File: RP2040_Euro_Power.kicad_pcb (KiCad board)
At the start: 2 copper layers, 110 x 110 mm, 150 parts, among them J1 Conn_01x40, J2 Conn_01x40, J3 Power, J4 USB C/USB 2.0, J5 Conn_01x03_Pin, SW1 SW_BOOT, SW2 SW_RESET, U1 78L05_SOT89, U101 TL431A, U2 W25Q128JVS, U4 AMS1117-3.3, U5 RP2040, U7 TL072, Y1 Crystal_12MHz_4Pin

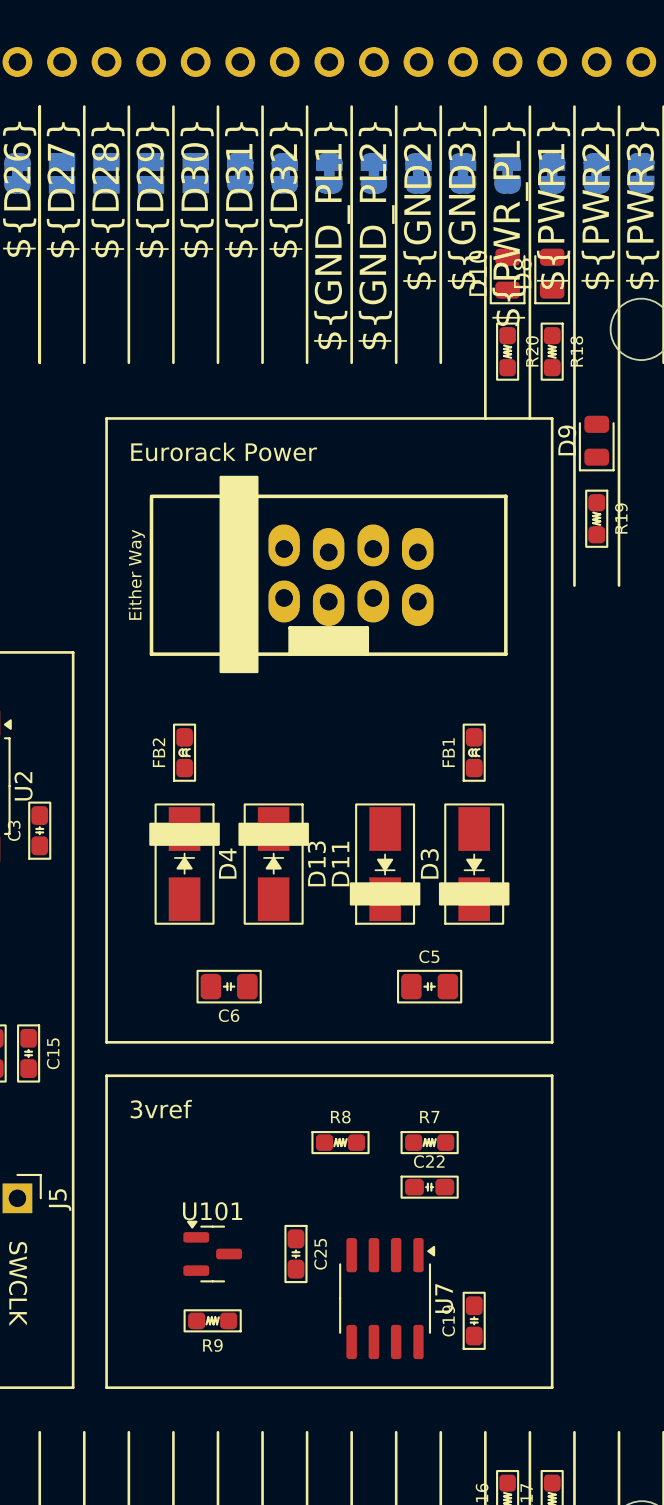
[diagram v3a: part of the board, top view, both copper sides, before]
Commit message: Second op amp used. Ready for routing
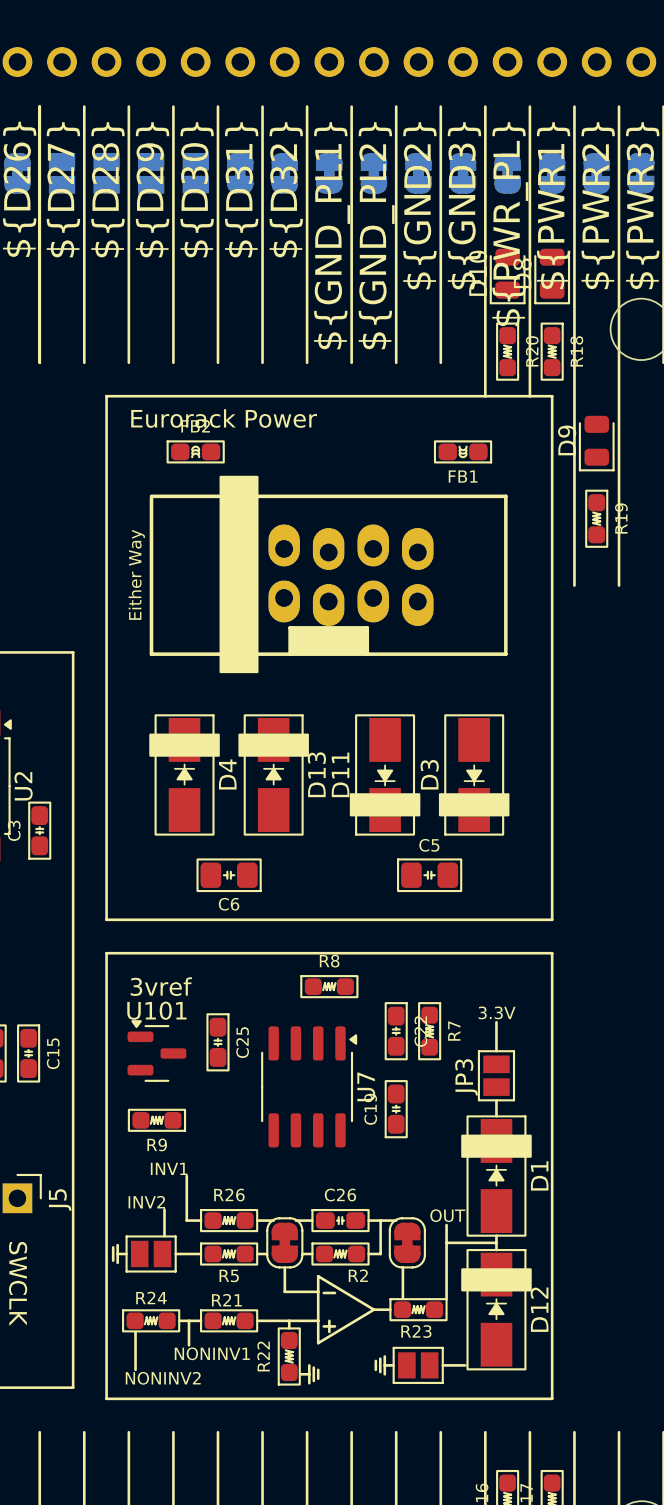
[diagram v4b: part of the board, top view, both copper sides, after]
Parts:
- added C26: DNP, winterbloom:C_0603_HandSolder, F.Cu at (161.3, 109.7)
- added D1: D_Schottky, winterbloom:D_SMA, F.Cu at (170.2, 107.1)
- added D12: D_Schottky, winterbloom:D_SMA, F.Cu at (170.2, 114.8)
- added JP1: Jumper_Closed, Jumper:SolderJumper-2_P1.3mm_Bridged_RoundedPad1.0x1.5mm, F.Cu at (158.2, 111.0)
- added JP2: SolderJumper_2_Open, Jumper:SolderJumper-2_P1.3mm_Open_Pad1.0x1.5mm, F.Cu at (150.5, 111.6)
- added JP201: Jumper_Closed, Jumper:SolderJumper-2_P1.3mm_Bridged_RoundedPad1.0x1.5mm, F.Cu at (165.2, 111.0)
- added JP3: SolderJumper_2_Open, Jumper:SolderJumper-2_P1.3mm_Open_Pad1.0x1.5mm, F.Cu at (170.2, 101.4)
- added JP4: SolderJumper_2_Open, Jumper:SolderJumper-2_P1.3mm_Open_Pad1.0x1.5mm, F.Cu at (165.8, 117.9)
- added R2: DNP, winterbloom:R_0603_HandSolder, F.Cu at (161.3, 111.6)
- added R21: DNP, winterbloom:R_0603_HandSolder, F.Cu at (155.0, 115.4)
- added R22: DNP, winterbloom:R_0603_HandSolder, F.Cu at (158.4, 117.4)
- added R23: DNP, winterbloom:R_0603_HandSolder, F.Cu at (165.8, 114.8)
- added R24: DNP, winterbloom:R_0603_HandSolder, F.Cu at (150.5, 115.4)
- added R26: DNP, winterbloom:R_0603_HandSolder, F.Cu at (155.0, 109.7)
- added R5: DNP, winterbloom:R_0603_HandSolder, F.Cu at (155.0, 111.6)
- moved FB1 17.2 mm to (168.3, 65.9), turned to 180 degrees
- moved FB2 17.2 mm to (153.1, 65.9), turned to 0 degrees
- moved C19 12.9 mm to (164.5, 103.3)
- moved C25 12.9 mm to (154.4, 99.5)
- moved U7 12.9 mm to (159.4, 102.1)
- moved R9 11.9 mm to (150.9, 104.0)
- moved U101 11.9 mm to (150.9, 100.2)
- moved C22 9.09 mm to (164.5, 98.9), turned to -90 degrees
- moved R8 8.91 mm to (160.7, 96.3)
- moved C5 6.35 mm to (166.4, 90.0)
- moved C6 6.35 mm to (155.0, 90.0)
- moved R7 6.35 mm to (166.4, 98.9), turned to -90 degrees
- moved D11 5.08 mm to (163.9, 84.3)
- moved D13 5.08 mm to (157.5, 84.3)
- moved D3 5.08 mm to (169.0, 84.3)
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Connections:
- U2 pad 1: Net-(U2-~{CS}) -> QSPI_CS
- U5 pad 56: Net-(U2-~{CS}) -> QSPI_CS
- U7 pad 5: GND_PLANE -> Net-(U7B-+)
- U7 pad 6: Net-(U7B--) -> Net-(JP1-A)
- U7 pad 7: Net-(U7B--) -> Net-(JP201-A)
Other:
- board text added: "3.3V"
- board text added: "INV1"
- board text added: "INV2"
- board text added: "NONINV1"
- board text added: "NONINV2"
- board text added: "OUT"

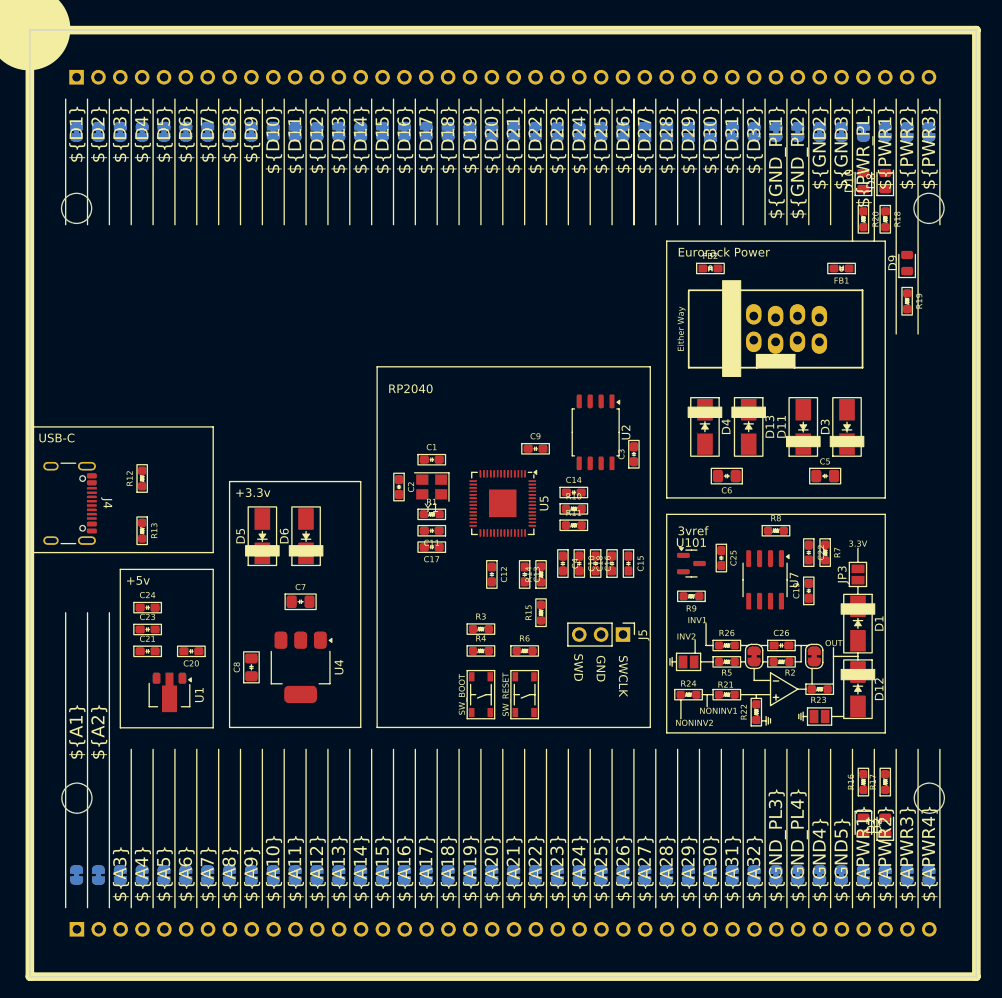
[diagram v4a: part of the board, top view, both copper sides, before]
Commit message: First draft of routing done. Still need to clean everything up, but it passes DRC.
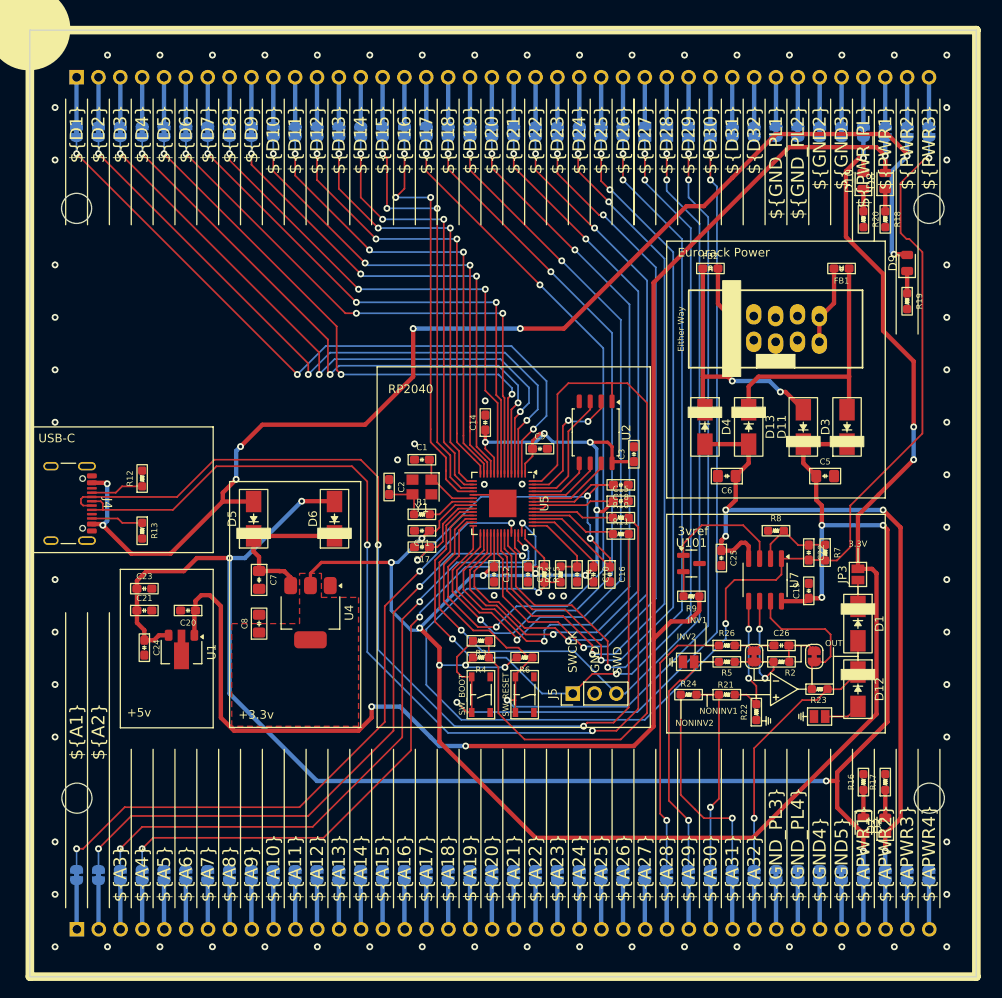
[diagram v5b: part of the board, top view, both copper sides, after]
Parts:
- moved C14 13.1 mm to (126.9, 83.8), turned to 90 degrees
- moved C18 9.20 mm to (142.7, 91.0), turned to 180 degrees
- moved J5 9.01 mm to (137.1, 115.3), turned to 90 degrees
- moved C15 7.29 mm to (142.7, 92.9), turned to 0 degrees
- moved U4 6.45 mm to (106.6, 105.9)
- moved R10 5.55 mm to (142.7, 94.8)
- moved R11 5.55 mm to (142.7, 96.7)
- moved C7 5.45 mm to (100.6, 102.1), turned to -90 degrees
- moved U1 5.19 mm to (91.6, 110.4)
- moved C8 5.16 mm to (100.6, 107.1)
- moved C20 4.76 mm to (92.4, 105.6)
- moved C21 4.76 mm to (87.3, 105.6)
- moved C23 4.76 mm to (87.3, 103.1)
- moved C24 4.67 mm to (87.3, 109.9), turned to -90 degrees
- moved R15 4.46 mm to (133.8, 101.4), turned to -90 degrees
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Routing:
- net IOVDD: track 0.00 -> 308.1 mm, vias 0 -> 16
- net APWR1: track 0.00 -> 207.4 mm, vias 0 -> 7
- net PWR1: track 0.00 -> 174.3 mm, vias 0 -> 3
- net PWR2: track 0.00 -> 149.8 mm, vias 0 -> 8
- net 3VREF: track 0.00 -> 142.9 mm, vias 0 -> 3
- net D29: track 0.00 -> 118.0 mm, vias 0 -> 3
- net USBD+: track 0.00 -> 116.0 mm, vias 0 -> 2
- net USBD-: track 0.00 -> 113.1 mm, vias 0 -> 2
- net D27: track 0.00 -> 110.2 mm, vias 0 -> 4
- net D28: track 0.00 -> 108.7 mm, vias 0 -> 3
- net BOOT: track 0.00 -> 105.1 mm, vias 0 -> 3
- net D26: track 0.00 -> 92.1 mm, vias 0 -> 3
- net D20: track 0.00 -> 91.6 mm, vias 0 -> 3
- net D17: track 0.00 -> 91.4 mm, vias 0 -> 3
- net QSPI_CS: track 0.00 -> 91.3 mm
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- added copper zone on F.Cu, net IOVDD

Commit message: Loom RP2040 V1 Ordered
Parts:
- JP101, JP102, JP103, JP104, JP105, JP106, JP107, JP108, JP109, JP110, JP111, JP112, JP113, JP114, JP115, JP116, JP117, JP118, JP119, JP120, JP121, JP122, JP123, JP124, JP125, JP126, JP131, JP132, JP133, JP134, JP135, JP136, JP137, JP138, JP139, JP140, JP141, JP142, JP143, JP144, JP145, JP146, JP147, JP148, JP149, JP150, JP151, JP152, JP153, JP154, JP155, JP156, JP157, JP158, JP159, JP160, JP161, JP162, JP163, JP164, JP165, JP166, JP167, JP168, JP169, JP170, JP171, JP172, JP173, JP174, JP175, JP176, JP177, JP178, JP179, JP180: footprint Jumper:SolderJumper-2_P1.3mm_Bridged_RoundedPad1.0x1.5mm -> Decapod_Devices:SolderJumper-2_P1.3mm_Bridged_RoundedPad1.0x1.5mm
- JP127, JP128, JP129, JP130: footprint Jumper:SolderJumper-2_P1.3mm_Open_Pad1.0x1.5mm -> Decapod_Devices:SolderJumper-2_P1.3mm_Open_Pad1.0x1.5mm
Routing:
- net PWR2: track 149.8 -> 145.3 mm
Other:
- board text added: "Add more GND Vias clean up ref des add any silk markings? add test points?"
- board text added: "TODO"

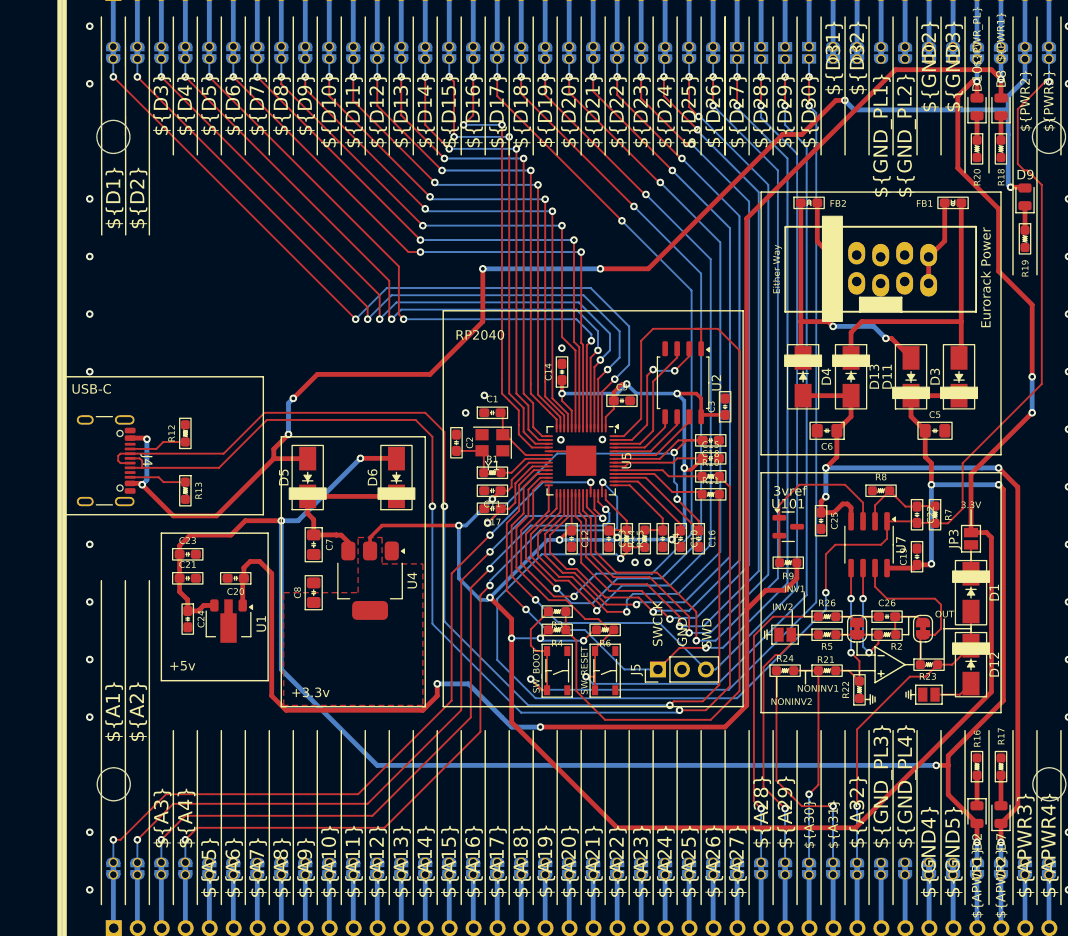
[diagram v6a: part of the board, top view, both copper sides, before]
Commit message: Moved buttons to the side, disconnected opamp
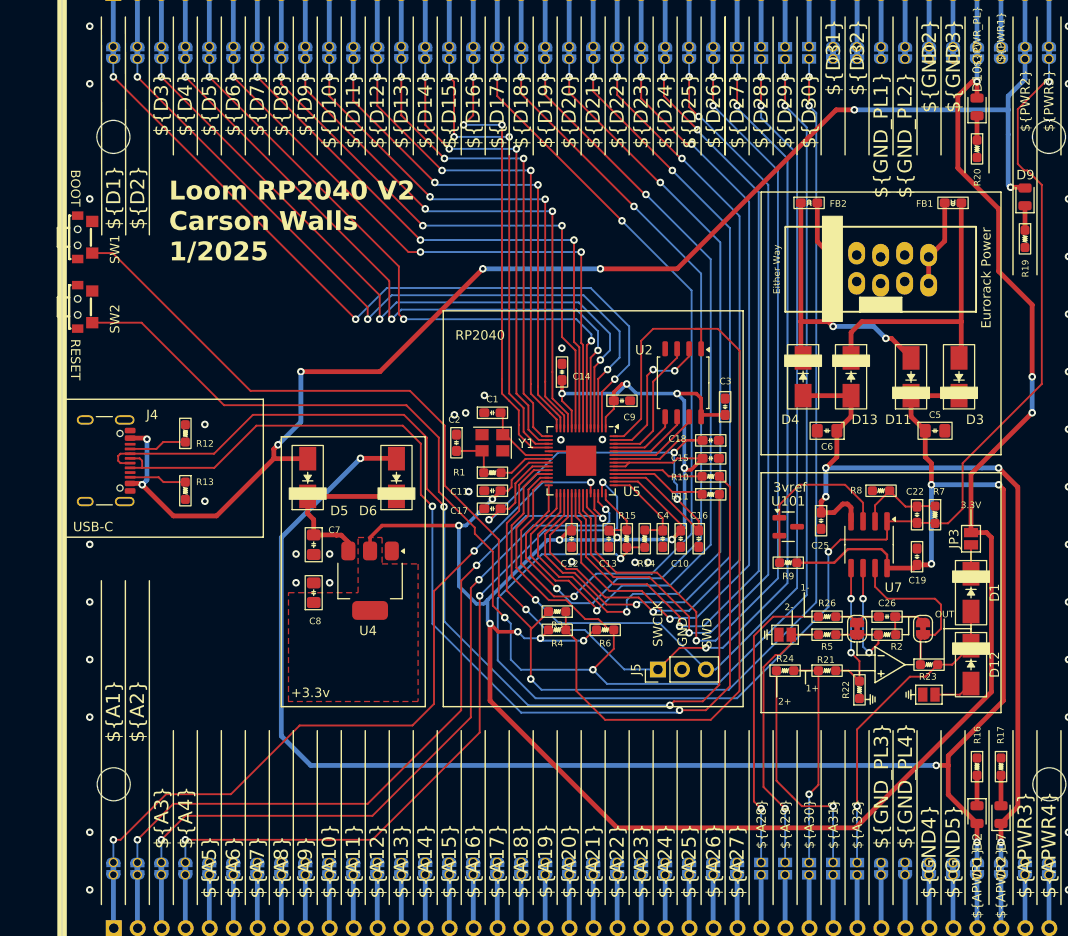
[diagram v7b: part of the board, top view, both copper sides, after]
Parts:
- removed C20, C21, C23, C24: 100n, winterbloom:C_0603_HandSolder
- removed D8: 5v, LED_SMD:LED_0805_2012Metric
- removed R18: 1k, winterbloom:R_0603_HandSolder
- removed U1: 78L05_SOT89, Package_TO_SOT_SMD:SOT-89-3
- JP168, JP169, JP170, JP171, JP172: value ~ -> SolderJumper_2_Open; footprint Decapod_Devices:SolderJumper-2_P1.3mm_Bridged_RoundedPad1.0x1.5mm -> Decapod_Devices:SolderJumper-2_P1.3mm_Open_Pad1.0x1.5mm
- R16, R17: value 3.3k -> 10k
- R19: value 1k -> 3.3k
- R20: value 470R -> 1k
- SW1: value SW_BOOT -> BOOT; footprint winterbloom:Tactile_Switch_4.2mm -> Decapod_Devices:SW-SMD_TS24CA
- SW2: value SW_RESET -> RESET; footprint winterbloom:Tactile_Switch_4.2mm -> Decapod_Devices:SW-SMD_TS24CA
- moved SW1 67.9 mm to (76.4, 69.5)
- moved SW2 67.2 mm to (76.4, 76.9)
- turned JP168 to 90 degrees
- turned JP169 to 90 degrees
- turned JP170 to 90 degrees
- turned JP171 to 90 degrees
- turned JP172 to 90 degrees
- turned R16 to -90 degrees
- turned R17 to -90 degrees
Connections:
- JP168 pad 1: A28 -> Net-(J2-Pin_28)
- JP168 pad 2: Net-(J2-Pin_28) -> A28
- JP169 pad 1: A29 -> Net-(J2-Pin_29)
- JP169 pad 2: Net-(J2-Pin_29) -> A29
- JP170 pad 1: A30 -> Net-(J2-Pin_30)
- JP170 pad 2: Net-(J2-Pin_30) -> A30
- JP171 pad 1: A31 -> Net-(J2-Pin_31)
- JP171 pad 2: Net-(J2-Pin_31) -> A31
- JP172 pad 1: A32 -> Net-(J2-Pin_32)
- JP172 pad 2: Net-(J2-Pin_32) -> A32
- R16 pad 1: Net-(D2-K) -> GND_PLANE
- R16 pad 2: GND_PLANE -> Net-(D2-K)
- R17 pad 1: Net-(D7-A) -> GND_PLANE
- R17 pad 2: GND_PLANE -> Net-(D7-A)
- R9 pad 1: PWR1 -> APWR1
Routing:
- net PWR1: track 174.3 -> 0.00 mm, vias 3 -> 0
- net D29: track 118.0 -> 192.0 mm, vias 3 -> 4
- net BOOT: track 105.1 -> 170.5 mm
- net APWR1: track 207.4 -> 200.0 mm, vias 7 -> 6
- net IOVDD: track 308.1 -> 311.7 mm
- net PWR2: track 145.3 -> 142.3 mm
- net Net-(D8-K): track 2.59 -> 0.00 mm
- net USBD+: track 116.0 -> 114.4 mm
- net USBD-: track 113.1 -> 111.5 mm
- net A1: track 77.7 -> 76.8 mm
- net DVDD: track 67.5 -> 66.8 mm
- net GND_PLANE: vias 70 -> 75
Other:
- board text added: "1+"
- board text added: "1-"
- board text added: "2+"
- board text added: "2-"
- board text added: "Loom RP2040 V2 Carson Walls 1/2025"
- board text removed: "+5v"
- board text removed: "INV1"
- board text removed: "INV2"
- board text removed: "NONINV1"
- board text removed: "NONINV2"
